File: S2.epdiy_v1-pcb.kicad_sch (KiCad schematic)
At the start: 78 parts, among them J1 USB_C_Receptacle_USB2.0, J2 Jack-DC, P1 CONN_02X13, P3 CONN_02X13, SW1 RESET, SW2 BOOT, U1 MCP1700-1202E_SOT23, U11 TP4056, U2 ESP32-S2-WROVER, U3 TPS651851RSLR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

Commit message: Update net and schema
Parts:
- removed P3: CONN_02X13, Connector_PinHeader_2.54mm:PinHeader_2x13_P2.54mm_Vertical, symbol Connector_Generic:Conn_02x13_Odd_Even
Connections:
- net IO08 is gone; now on net SCL: P1.18 (Pin_18), U2.11 (IO08)
- net IO09 is gone; now on net SDA: P1.20 (Pin_20), U2.12 (IO09)
- net GND: now also C13.2; no longer C13.1
- net TPS_PWR_GOOD: now also P1.26 (Pin_26)
- net TPS_VCOM_CTRL: now also U2.13 (IO10); no longer U2.20 (IO17)
- net TPS_nINT: now also U2.14 (IO11); no longer U2.39 (IO45)
- net at R1.2, SW1.1, U2.41 (EN): now also C13.1; no longer C13.2
- net IO10 renamed IO17
- net IO17: now also U2.20 (IO17); no longer U2.13 (IO10)
- net IO11 renamed IO45
- net IO45: now also U2.39 (IO45); no longer U2.14 (IO11)
- no-connect marks 41 -> 20
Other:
- moved on the sheet: C13, R1, R8

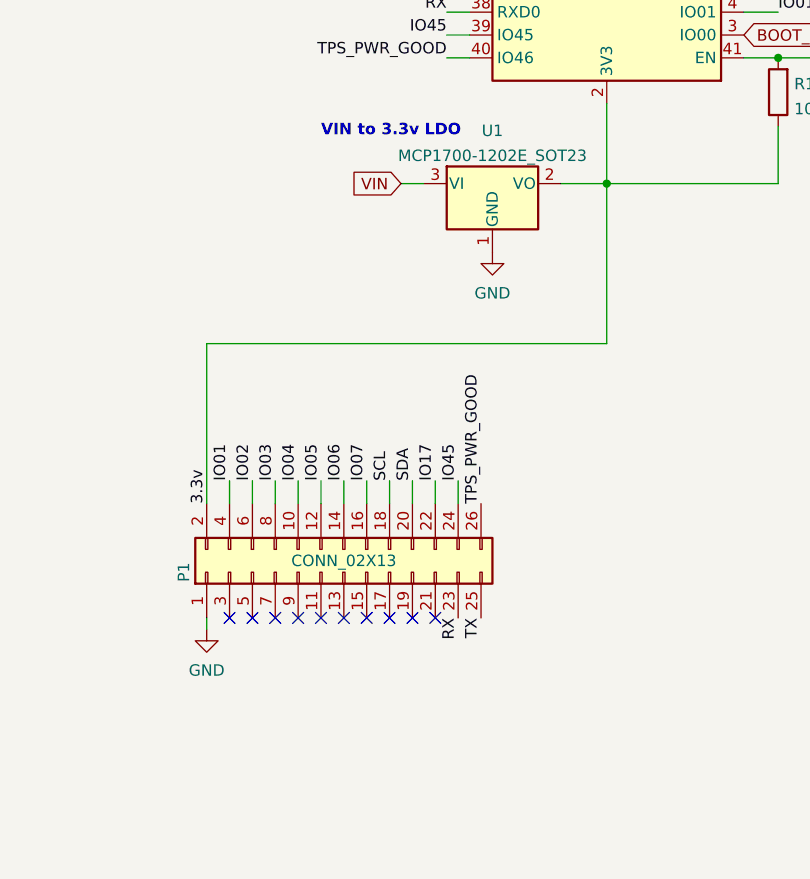
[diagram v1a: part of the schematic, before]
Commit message: Routing v1. Pending ERC pass
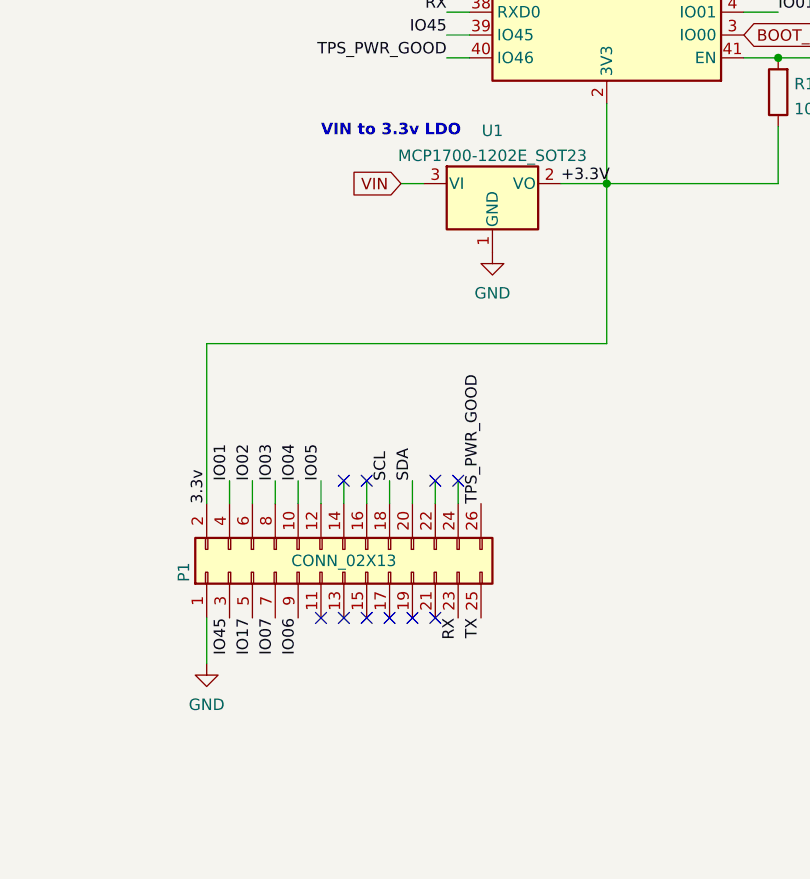
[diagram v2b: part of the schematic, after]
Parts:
- U3: footprint footprint:TPS651851RSLR -> RSL48_4P4X4P4; symbol TPS651851RSLR:TPS651851RSLR -> TPS65185:TPS651851RSLR
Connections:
- net 3.3v is gone; now on net +3.3V: P1.2 (Pin_2), R1.1, U1.2 (VO), U2.2 (3V3)
- net IO06: now also P1.9 (Pin_9); no longer P1.14 (Pin_14)
- net IO07: now also P1.7 (Pin_7); no longer P1.16 (Pin_16)
- net IO17: now also P1.5 (Pin_5); no longer P1.22 (Pin_22)
- net IO45: now also P1.3 (Pin_3); no longer P1.24 (Pin_24)
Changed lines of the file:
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@@
   )
   (no_connect (at 378.46 41.91))
-  (no_connect (at 90.17 153.67))
-  (no_connect (at 92.71 153.67))
-  (no_connect (at 95.25 153.67))
+  (no_connect (at 102.87 138.43))
   (no_connect (at 107.95 153.67))
   (no_connect (at 110.49 153.67))
   (no_connect (at 113.03 153.67))
-  (no_connect (at 97.79 153.67))
-  (no_connect (at 100.33 153.67))
   (no_connect (at 102.87 153.67))
   (no_connect (at 105.41 153.67))
@@
   (no_connect (at 114.3 55.88))
   (no_connect (at 300.99 180.34))
+  (no_connect (at 113.03 138.43))
+  (no_connect (at 100.33 153.67))
   (no_connect (at 76.2 66.04))
   (no_connect (at 76.2 63.5))
   (no_connect (at 250.19 180.34))
   (no_connect (at 250.19 185.42))
+  (no_connect (at 105.41 138.43))
+  (no_connect (at 115.57 138.43))
   (wire (pts (xy 132.08 34.29) (xy 132.08 38.1))
     (stroke (width 0) (type default) (color 0 0 0 0))
@@
     (stroke (width 0) (type default) (color 0 0 0 0))
   )
-  (wire (pts (xy 87.63 153.67) (xy 87.63 154.94))
+  (wire (pts (xy 87.63 153.67) (xy 87.63 158.75))
     (stroke (width 0) (type default) (color 0 0 0 0))
   )
@@
     (effects (font (size 1.27 1.27)) (justify left bottom))
   )
-  (label "IO07" (at 105.41 138.43 90)
-    (effects (font (size 1.27 1.27)) (justify left bottom))
-  )
   (label "TPS_nINT" (at 151.13 60.96 0)
     (effects (font (size 1.27 1.27)) (justify left bottom))
   )
+  (label "IO07" (at 95.25 153.67 270)
+    (effects (font (size 1.27 1.27)) (justify right bottom))
+  )
   (label "EP_D6" (at 114.3 73.66 180)
     (effects (font (size 1.27 1.27)) (justify right bottom))
@@
     (effects (font (size 1.27 1.27)) (justify left bottom))
   )
+  (label "IO45" (at 90.17 153.67 270)
+    (effects (font (size 1.27 1.27)) (justify right bottom))
+  )
+  (label "IO17" (at 92.71 153.67 270)
+    (effects (font (size 1.27 1.27)) (justify right bottom))
+  )
   (label "-15V" (at 57.15 189.23 0)
     (effects (font (size 1.27 1.27)) (justify left bottom))
@@
     (effects (font (size 1.27 1.27)) (justify left bottom))
   )
+  (label "IO06" (at 97.79 153.67 270)
+    (effects (font (size 1.27 1.27)) (justify right bottom))
+  )
   (label "EP_LE" (at 57.15 212.09 0)
     (effects (font (size 1.27 1.27)) (justify left bottom))
@@
     (effects (font (size 1.27 1.27)) (justify right bottom))
   )
-  (label "IO17" (at 113.03 138.43 90)
-    (effects (font (size 1.27 1.27)) (justify left bottom))
-  )
   (label "TX" (at 114.3 83.82 180)
     (effects (font (size 1.27 1.27)) (justify right bottom))
   )
-  (label "IO06" (at 102.87 138.43 90)
-    (effects (font (size 1.27 1.27)) (justify left bottom))
-  )
   (label "3.3v" (at 87.63 140.97 90)
     (effects (font (size 1.27 1.27)) (justify left bottom))
@@
     (effects (font (size 1.27 1.27)) (justify right bottom))
   )
+  (label "+3.3V" (at 127 105.41 0)
+    (effects (font (size 1.27 1.27)) (justify left bottom))
+  )
   (label "+22V" (at 369.57 184.15 180)
     (effects (font (size 1.27 1.27)) (justify right bottom))
@@
     (effects (font (size 1.27 1.27)) (justify left bottom))
   )
-  (label "IO45" (at 115.57 138.43 90)
-    (effects (font (size 1.27 1.27)) (justify left bottom))
-  )
   (label "VNEG_IN" (at 240.03 193.04 0)
     (effects (font (size 1.27 1.27)) (justify left bottom))
@@
     (pin "9")
   )
-  (symbol (lib_id "TPS651851RSLR:TPS651851RSLR") (at 250.19 154.94 0) (unit 1)
+  (symbol (lib_id "TPS65185:TPS651851RSLR") (at 250.19 154.94 0) (unit 1)
     (in_bom yes) (on_board yes)
     (property "Reference" "U3" (id 0) (at 290.83 145.1102 0)
@@
       (effects (font (size 1.524 1.524)))
     )
-    (property "Footprint" "footprint:TPS651851RSLR" (id 2) (at 290.83 148.844 0)
+    (property "Footprint" "RSL48_4P4X4P4" (id 2) (at 276.86 148.844 0)
       (effects (font (size 1.524 1.524)) hide)
     )
@@
     (pin "1")
   )
-  (symbol (lib_id "power:GND") (at 87.63 154.94 0) (unit 1)
+  (symbol (lib_id "power:GND") (at 87.63 158.75 0) (unit 1)
     (in_bom yes) (on_board yes) (fields_autoplaced)
-    (property "Reference" "#PWR0103" (id 0) (at 87.63 161.29 0)
+    (property "Reference" "#PWR0103" (id 0) (at 87.63 165.1 0)
       (effects (font (size 1.27 1.27)) hide)
     )
-    (property "Value" "GND" (id 1) (at 87.63 159.5025 0))
-    (property "Footprint" "" (id 2) (at 87.63 154.94 0)
+    (property "Value" "GND" (id 1) (at 87.63 163.3125 0))
+    (property "Footprint" "" (id 2) (at 87.63 158.75 0)
       (effects (font (size 1.27 1.27)) hide)
     )
-    (property "Datasheet" "" (id 3) (at 87.63 154.94 0)
+    (property "Datasheet" "" (id 3) (at 87.63 158.75 0)
       (effects (font (size 1.27 1.27)) hide)
     )
@@
     )
     (path "/00000000-0000-0000-0000-0000607396d1"
-      (reference "U3") (unit 1) (value "TPS651851RSLR") (footprint "footprint:TPS651851RSLR")
+      (reference "U3") (unit 1) (value "TPS651851RSLR") (footprint "RSL48_4P4X4P4")
     )
     (path "/00000000-0000-0000-0000-000061320af7"

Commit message: Add 470uF C at LDO 3.3v output
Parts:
- added C15: C_Polarized, Capacitor_Tantalum_SMD:CP_EIA-7343-43_Kemet-X, symbol Device:C_Polarized
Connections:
- net +3.3V: now also C15.1
- net GND: now also C15.2
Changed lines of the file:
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@@
   (junction (at 320.04 146.05) (diameter 0) (color 0 0 0 0)
   )
+  (junction (at 128.27 105.41) (diameter 0) (color 0 0 0 0)
+  )
   (junction (at 321.31 214.63) (diameter 0) (color 0 0 0 0)
   )
@@
   (junction (at 313.69 146.05) (diameter 0) (color 0 0 0 0)
   )
+  (junction (at 119.38 114.3) (diameter 0) (color 0 0 0 0)
+  )
   (junction (at 120.65 232.41) (diameter 0) (color 0 0 0 0)
   )
@@
     (stroke (width 0) (type default) (color 0 0 0 0))
   )
+  (wire (pts (xy 119.38 116.84) (xy 119.38 114.3))
+    (stroke (width 0) (type default) (color 0 0 0 0))
+  )
   (polyline (pts (xy 208.28 71.12) (xy 259.08 71.12))
     (stroke (width 0) (type default) (color 0 0 0 0))
@@
     (stroke (width 0) (type default) (color 0 0 0 0))
   )
-  (wire (pts (xy 127 105.41) (xy 132.08 105.41))
+  (wire (pts (xy 127 105.41) (xy 128.27 105.41))
     (stroke (width 0) (type default) (color 0 0 0 0))
   )
@@
     (stroke (width 0) (type default) (color 0 0 0 0))
   )
+  (wire (pts (xy 119.38 114.3) (xy 119.38 113.03))
+    (stroke (width 0) (type default) (color 0 0 0 0))
+  )
   (wire (pts (xy 341.63 173.99) (xy 341.63 177.8))
     (stroke (width 0) (type default) (color 0 0 0 0))
@@
     (stroke (width 0) (type default) (color 0 0 0 0))
   )
+  (wire (pts (xy 119.38 114.3) (xy 128.27 114.3))
+    (stroke (width 0) (type default) (color 0 0 0 0))
+  )
   (wire (pts (xy 300.99 177.8) (xy 327.66 177.8))
     (stroke (width 0) (type default) (color 0 0 0 0))
@@
     (stroke (width 0) (type default) (color 0 0 0 0))
   )
+  (wire (pts (xy 128.27 106.68) (xy 128.27 105.41))
+    (stroke (width 0) (type default) (color 0 0 0 0))
+  )
   (wire (pts (xy 109.22 105.41) (xy 111.76 105.41))
     (stroke (width 0) (type default) (color 0 0 0 0))
@@
     (stroke (width 0) (type default) (color 0 0 0 0))
   )
+  (wire (pts (xy 128.27 105.41) (xy 132.08 105.41))
+    (stroke (width 0) (type default) (color 0 0 0 0))
+  )
   (wire (pts (xy 168.91 232.41) (xy 162.56 232.41))
     (stroke (width 0) (type default) (color 0 0 0 0))
@@
     (pin "2")
   )
+  (symbol (lib_id "Device:C_Polarized") (at 128.27 110.49 0) (unit 1)
+    (in_bom yes) (on_board yes)
+    (property "Reference" "C15" (id 0) (at 133.35 109.22 0)
+      (effects (font (size 1.27 1.27)) (justify left))
+    )
+    (property "Value" "C_Polarized" (id 1) (at 133.35 111.76 0)
+      (effects (font (size 1.27 1.27)) (justify left))
+    )
+    (property "Footprint" "Capacitor_Tantalum_SMD:CP_EIA-7343-43_Kemet-X" (id 2) (at 129.2352 114.3 0)
+      (effects (font (size 1.27 1.27)) hide)
+    )
+    (property "Datasheet" "https://datasheet.lcsc.com/lcsc/2004141707_KEMET-T491X477K010AT_C513339.pdf" (id 3) (at 128.27 110.49 0)
+      (effects (font (size 1.27 1.27)) hide)
+    )
+    (property "LCSC" "C513339" (id 4) (at 128.27 110.49 0)
+      (effects (font (size 1.27 1.27)) hide)
+    )
+    (pin "1")
+    (pin "2")
+  )
   (symbol (lib_id "Connector:Jack-DC") (at 229.87 85.09 0) (unit 1)
     (in_bom yes) (on_board yes) (fields_autoplaced)
@@
     (pin "1")
   )
-  (symbol (lib_id "power:GND") (at 119.38 113.03 0) (unit 1)
+  (symbol (lib_id "power:GND") (at 119.38 116.84 0) (unit 1)
     (in_bom yes) (on_board yes) (fields_autoplaced)
-    (property "Reference" "#PWR0107" (id 0) (at 119.38 119.38 0)
+    (property "Reference" "#PWR0107" (id 0) (at 119.38 123.19 0)
       (effects (font (size 1.27 1.27)) hide)
     )
-    (property "Value" "GND" (id 1) (at 119.38 117.5925 0))
-    (property "Footprint" "" (id 2) (at 119.38 113.03 0)
+    (property "Value" "GND" (id 1) (at 119.38 121.4025 0))
+    (property "Footprint" "" (id 2) (at 119.38 116.84 0)
       (effects (font (size 1.27 1.27)) hide)
     )
-    (property "Datasheet" "" (id 3) (at 119.38 113.03 0)
+    (property "Datasheet" "" (id 3) (at 119.38 116.84 0)
       (effects (font (size 1.27 1.27)) hide)
     )
@@
       (reference "C14") (unit 1) (value "0.1u") (footprint "Capacitor_SMD:C_0805_2012Metric")
     )
+    (path "/518dd289-dd09-499b-a959-5caca8e3196e"
+      (reference "C15") (unit 1) (value "C_Polarized") (footprint "Capacitor_Tantalum_SMD:CP_EIA-7343-43_Kemet-X")
+    )
     (path "/00000000-0000-0000-0000-00006783cbac"

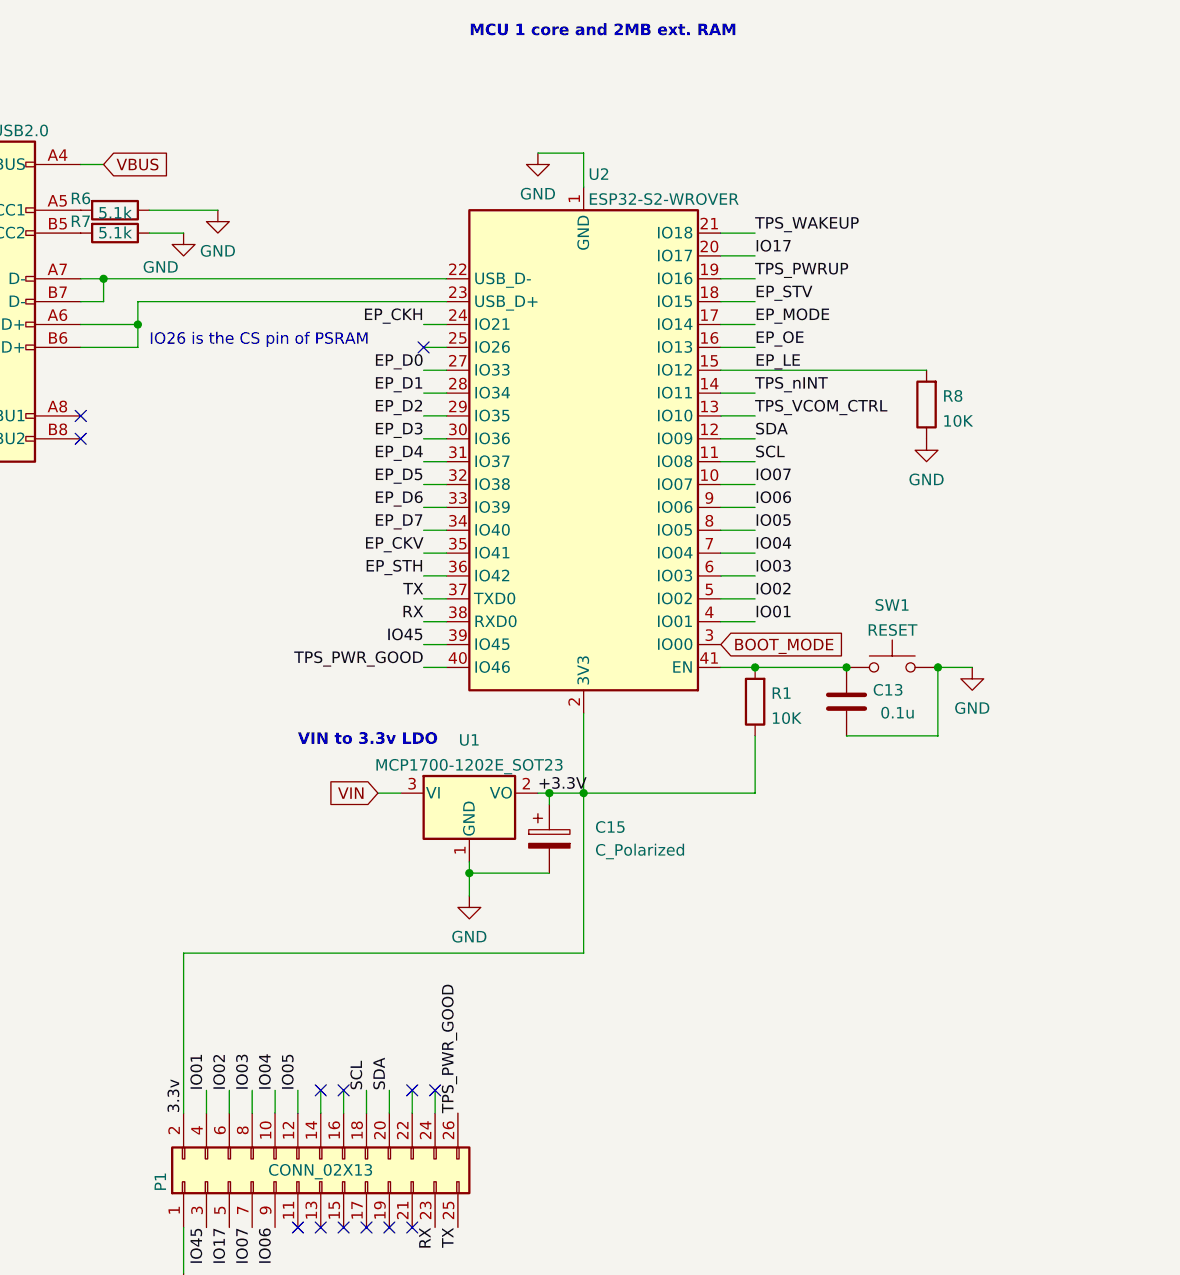
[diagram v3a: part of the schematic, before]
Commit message: I2C pullups
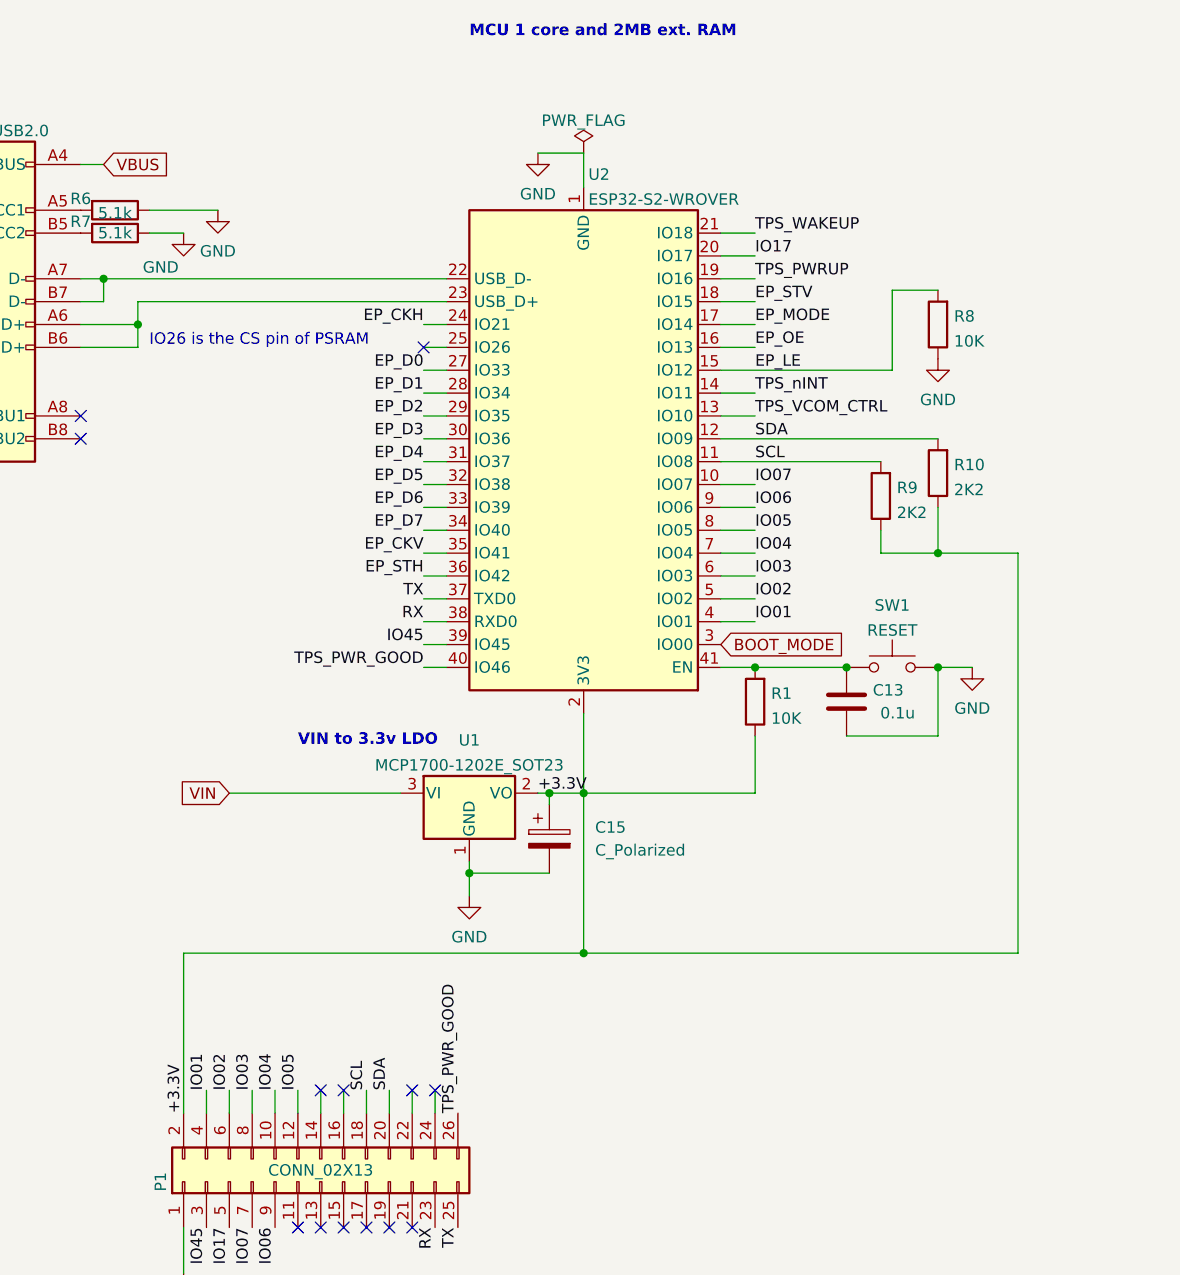
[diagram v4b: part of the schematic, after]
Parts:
- added R10, R9: 2K2, Resistor_SMD:R_0603_1608Metric, symbol Device:R
- U3: footprint RSL48_4P4X4P4 -> footprint:TPS651851RSLR
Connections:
- net +3.3V: now also R10.1, R9.1
- net SCL: now also R9.2
- net SDA: now also R10.2
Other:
- moved on the sheet: R8
